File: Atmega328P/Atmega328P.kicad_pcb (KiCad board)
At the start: 2 copper layers, 50.7 x 30.7 mm, 29 parts, among them J1 Conn_01x04_Pin, J2 Conn_01x09_Pin, J3 Conn_01x04_Pin, J4 Conn_02x03_Odd_Even, U1 24LC1025, U2 DS1337S_, U3 24LC1025, U4 ATMEGA328P-AU, Y1 32.768 KHz, Y2 16 MHz

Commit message: Rounting completed
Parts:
- moved BT1 0.88 mm to (82.4, 97.5), turned to 0 degrees
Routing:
- net GND: track 0.00 -> 164.3 mm, vias 0 -> 9
- net VCC: track 0.00 -> 141.9 mm
- net /SCL: track 0.00 -> 80.2 mm, vias 0 -> 6
- net /SDA: track 0.00 -> 52.9 mm, vias 0 -> 5
- net /RX: track 0.00 -> 44.1 mm, vias 0 -> 1
- net /TX: track 0.00 -> 43.2 mm, vias 0 -> 1
- net /MOSI: track 0.00 -> 35.7 mm, vias 0 -> 1
- net /RESET: track 0.00 -> 30.9 mm, vias 0 -> 2
- net /MISO: track 0.00 -> 25.5 mm, vias 0 -> 3
- net /D2: track 0.00 -> 19.1 mm, vias 0 -> 1
- net /D3: track 0.00 -> 17.3 mm, vias 0 -> 1
- net /D4: track 0.00 -> 17.0 mm, vias 0 -> 1
- net /D8: track 0.00 -> 12.5 mm, vias 0 -> 1
- net Net-(U4-PB6): track 0.00 -> 10.9 mm, vias 0 -> 2
- net /D7: track 0.00 -> 10.7 mm, vias 0 -> 1
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- added copper zone on B.Cu, net GND
- added copper zone on F.Cu, net VCC
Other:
- copper layers 2 -> 4
- board text removed: "V-1.0 Atmega328P Digital Pin"

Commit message: 4Layer PCB-production ready
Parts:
- added REF1: ESD-Logo_6.6x6mm_SilkScreen, Symbol:ESD-Logo_6.6x6mm_SilkScreen, B.Cu at (121.2, 105.2)
- added REF2: KiCad-Logo2_5mm_SilkScreen, Symbol:KiCad-Logo2_5mm_SilkScreen, B.Cu at (142.6, 105.2)
- moved BT1 36.1 mm to (118.6, 97.5)
- moved C1 36.1 mm to (156.9, 94.1)
- moved C2 36.1 mm to (123.2, 94.0)
- moved C3 36.1 mm to (123.2, 105.6)
- moved J1 36.1 mm to (149.5, 109.9)
- moved R1 36.1 mm to (148.9, 93.1)
- moved R2 36.1 mm to (156.9, 96.1)
- moved R3 36.1 mm to (154.8, 101.8)
- moved R4 36.1 mm to (156.8, 101.8)
- moved R5 36.1 mm to (148.9, 100.7)
- moved R7 36.1 mm to (148.9, 102.7)
- moved U1 36.1 mm to (138.3, 88.2)
- moved U2 36.1 mm to (150.9, 96.9)
- moved U4 36.1 mm to (131.4, 98.8)
- moved C4 36.1 mm to (138.0, 98.8)
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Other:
- board text added: "V-1.1 Atmega328P - Digital_Pin"

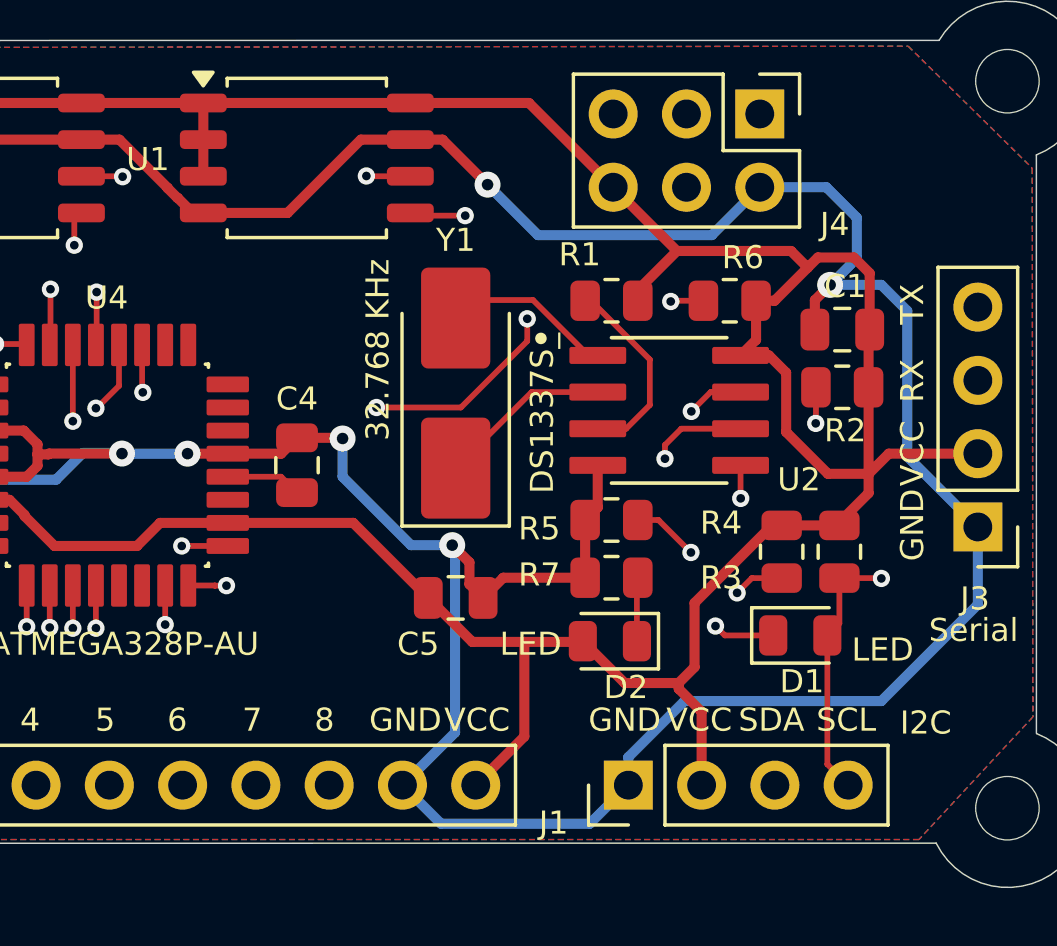
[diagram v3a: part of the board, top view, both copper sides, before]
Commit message: SCL Error - PCB Routing completed.
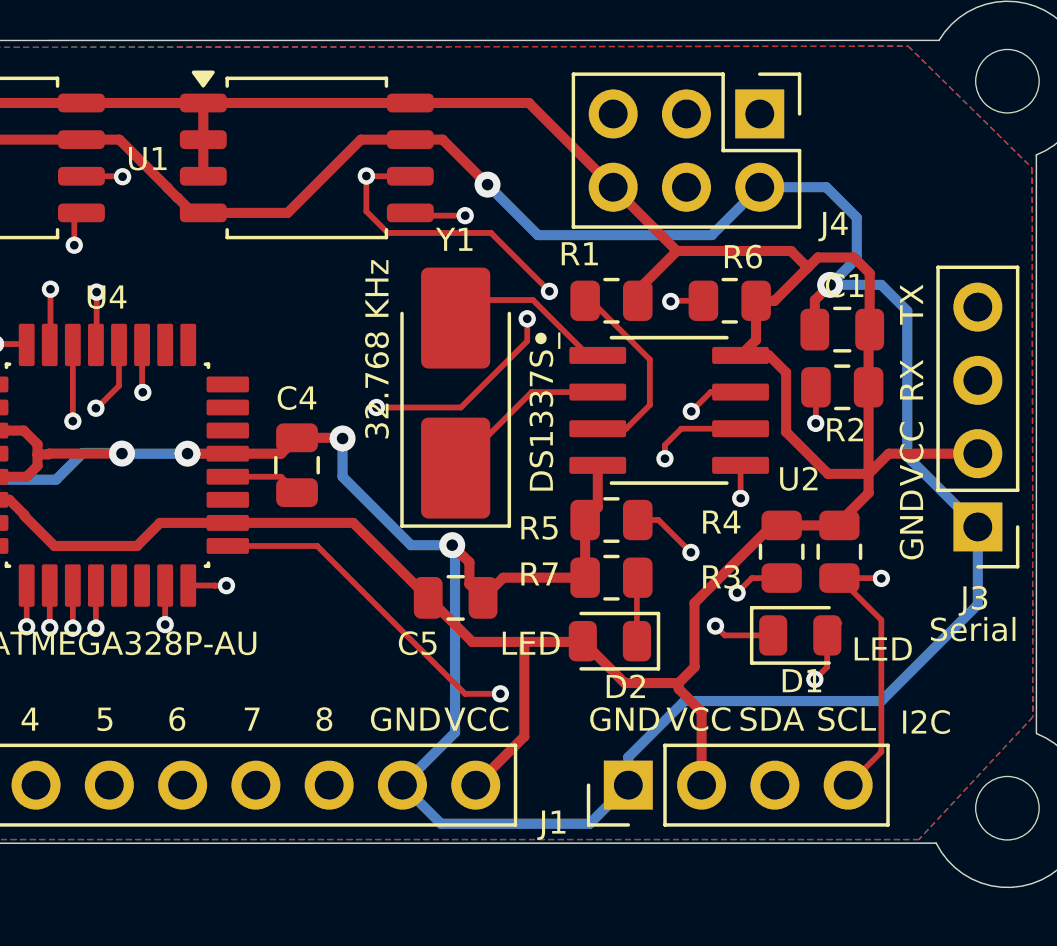
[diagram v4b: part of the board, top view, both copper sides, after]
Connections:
- D1 pad 2: /SCL -> /SCK
- J4 pad 3: /SCL -> /SCK
- U4 pad 17: /SCL -> /SCK
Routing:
- net /SCK: track 0.00 -> 51.6 mm, vias 0 -> 2
- net /SCL: track 80.2 -> 64.7 mm
